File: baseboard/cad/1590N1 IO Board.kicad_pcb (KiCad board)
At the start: 4 copper layers, 100 x 90 mm, 92 parts, among them J1 DC POWER JACK, J10 2P_HEADER, J11 2P_HEADER, J12 6-440054-2, J13 6-440054-2, J17 6-440054-2, J18 6-440054-2, J2 1/4" JACK, STEREO, J3 6-440054-2, J5 1/4" JACK, STEREO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

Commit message: swapped micro and started layout
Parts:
- removed U11, U12: DRV8212P, Package_SON:WSON-8-1EP_2x2mm_P0.5mm_EP0.9x1.6mm
- added C33: 100nF, Capacitor_SMD:C_1206_3216Metric, F.Cu at (123.3, 120.6)
- added C34: 10nF, Capacitor_SMD:C_1206_3216Metric, F.Cu at (125.2, 112.7)
- added C35: 100nF, Capacitor_SMD:C_1206_3216Metric, F.Cu at (127.6, 113.2)
- added C36: 22μF, Capacitor_SMD:C_0805_2012Metric, F.Cu at (129.8, 112.1)
- added D9: PESD12VL2BT,215, Package_TO_SOT_SMD:SOT-23, F.Cu at (121.2, 113.1)
- added J16: Conn_01x04_Pin, Connector_PinHeader_2.54mm:PinHeader_1x04_P2.54mm_Vertical, F.Cu at (117.4, 109.3)
- added SW3: SW_DIP_x01, Button_Switch_SMD:SW_Push_SPST_NO_Alps_SKRK, F.Cu at (133.4, 114.5)
- added U3: DRV8833RTY, Package_DFN_QFN:Texas_S-PWQFN-N16_EP2.1x2.1mm_ThermalVias, F.Cu at (128.0, 107.7)
- added Y1: 830054236, Crystal:Crystal_SMD_3215-2Pin_3.2x1.5mm, F.Cu at (131.2, 123.2)
- U8: footprint Package_DFN_QFN:DFN-10-1EP_3x3mm_P0.5mm_EP1.65x2.38mm -> Package_DFN_QFN:DFN-10-1EP_3x3mm_P0.5mm_EP1.65x2.38mm_ThermalVias
- moved U10 119.6 mm to (128.0, 120.5), turned to 180 degrees
- moved C32 111.8 mm to (132.7, 119.8), turned to 180 degrees
- moved C30 109.9 mm to (134.0, 124.5)
- moved C31 109.3 mm to (134.0, 122.0)
- moved R2 100.3 mm to (109.0, 95.4), turned to -90 degrees
- moved C4 99.9 mm to (107.3, 95.4), turned to 90 degrees
- moved F1 95.2 mm to (124.0, 87.5), turned to 90 degrees
- moved F2 94.1 mm to (126.4, 87.5), turned to 90 degrees
- moved C8 92.2 mm to (111.3, 96.1), turned to -90 degrees
- moved C7 88.9 mm to (113.8, 96.1), turned to -90 degrees
- moved C6 85.6 mm to (116.2, 96.1), turned to -90 degrees
- moved D2 84.7 mm to (124.8, 83.1), turned to -90 degrees
- moved D4 84.4 mm to (130.2, 85.2), turned to 90 degrees
- moved K1 82.0 mm to (123.2, 97.6), turned to 90 degrees
- moved K2 71.7 mm to (132.8, 97.6), turned to 90 degrees
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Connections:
- D1 pad 1: Net-(D1-A1) -> GND
- D2 pad 1: Net-(D2-A1) -> /Input Output/DC_IN+
- D3 pad 1: Net-(D3-A1) -> GND
- D4 pad 3: Net-(D4-+) -> DC_IN
- J1 pad 3: Net-(J1-Pad3) -> /Input Output/BATT_SW_A
- J2 pad R: Net-(J2-PadR) -> /Input Output/BATT_SW_B
- J2 pad RN: Net-(J2-PadR) -> /Input Output/BATT_SW_B
- U10 pad 10: unconnected-(U10-PA7-Pad10) -> +9V_EN
- U10 pad 11: unconnected-(U10-PB1-Pad11) -> -9V_EN
- U10 pad 16: SWDIO -> SWDCK
- U10 pad 17: SWDCK -> SWDIO
- U10 pad 6: /Microcontroller/H-BRIDGE1_IN1 -> /Microcontroller/H-BRIDGE2_IN2
- U10 pad 7: /Microcontroller/H-BRIDGE1_IN2 -> /Microcontroller/H-BRIDGE2_IN1
- U10 pad 8: /Microcontroller/H-BRIDGE2_IN1 -> /Microcontroller/H-BRIDGE1_IN2
- U10 pad 9: /Microcontroller/H-BRIDGE2_IN2 -> /Microcontroller/H-BRIDGE1_IN1
- U9 pad 10: +Vsw -> -9V_EN
- U9 pad 12: +Vsw -> +9V_EN
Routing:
- net SWDIO: track 0.00 -> 25.8 mm
- net /Microcontroller/K1_COIL_A: track 0.00 -> 22.3 mm
- net /Microcontroller/K2_COIL_A: track 0.00 -> 22.3 mm
- net SWDCK: track 0.00 -> 21.3 mm
- net /Microcontroller/H-BRIDGE1_IN1: track 0.00 -> 14.9 mm
- net GND: track 0.00 -> 14.7 mm, vias 0 -> 14
- net /Microcontroller/H-BRIDGE1_IN2: track 0.00 -> 14.1 mm
- net /Microcontroller/H-BRIDGE2_IN2: track 0.00 -> 13.1 mm
- net /Microcontroller/H-BRIDGE2_IN1: track 0.00 -> 12.5 mm
- net /Microcontroller/K2_COIL_B: track 0.00 -> 11.1 mm
- net /Microcontroller/K1_COIL_B: track 0.00 -> 11.1 mm
- net /Input Output/DC_IN+: track 0.00 -> 10.1 mm
- net /Switching/BYPASS_1: track 0.00 -> 9.72 mm
- net /Switching/BYPASS_2: track 0.00 -> 9.72 mm
- net /Input Output/DC_IN_FUSED-: track 0.00 -> 8.54 mm
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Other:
- board size 100 x 90 mm -> 58 x 77 mm
- board text added: "3V3"
- board text added: "CLK"
- board text added: "GND"
- board text added: "IO"
- board text added: "SWD"

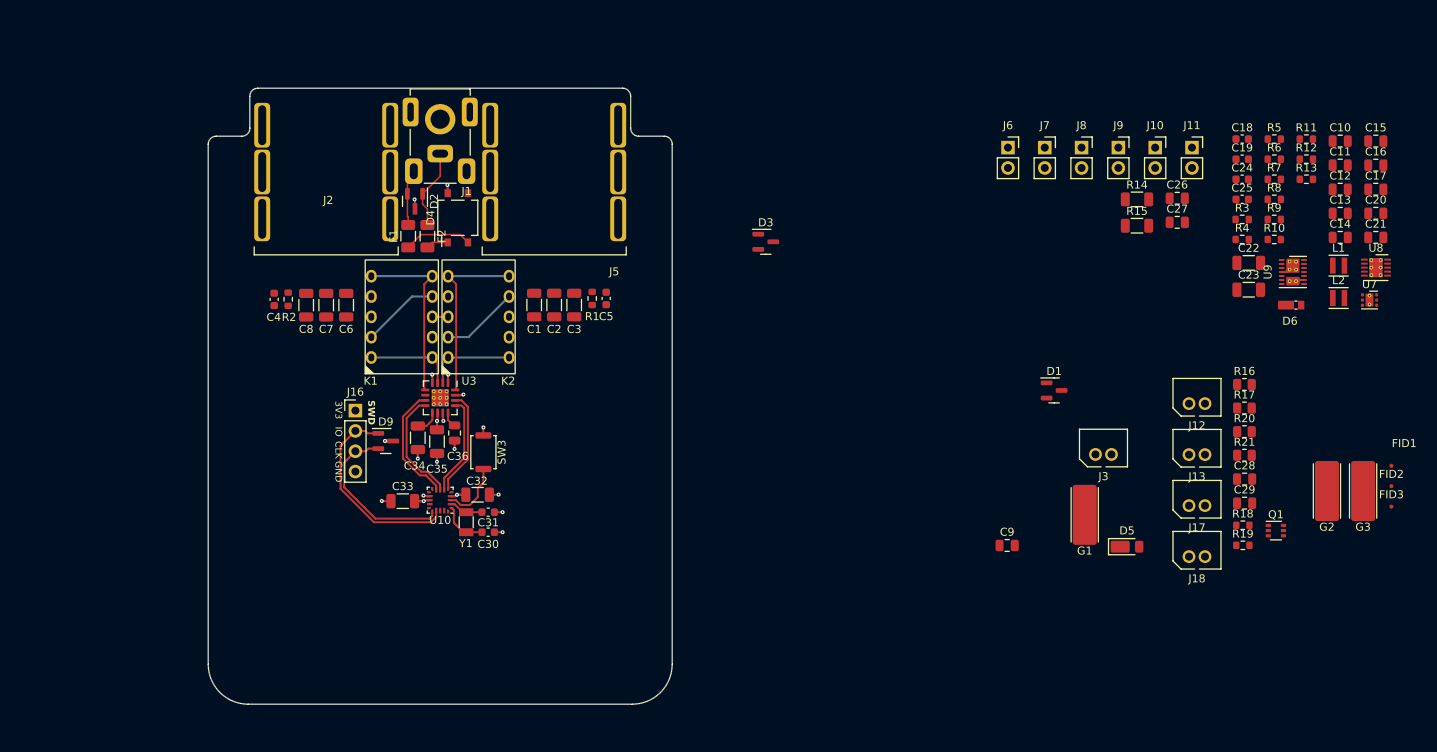
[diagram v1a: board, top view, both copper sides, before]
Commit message: placed components and finished new micro hw
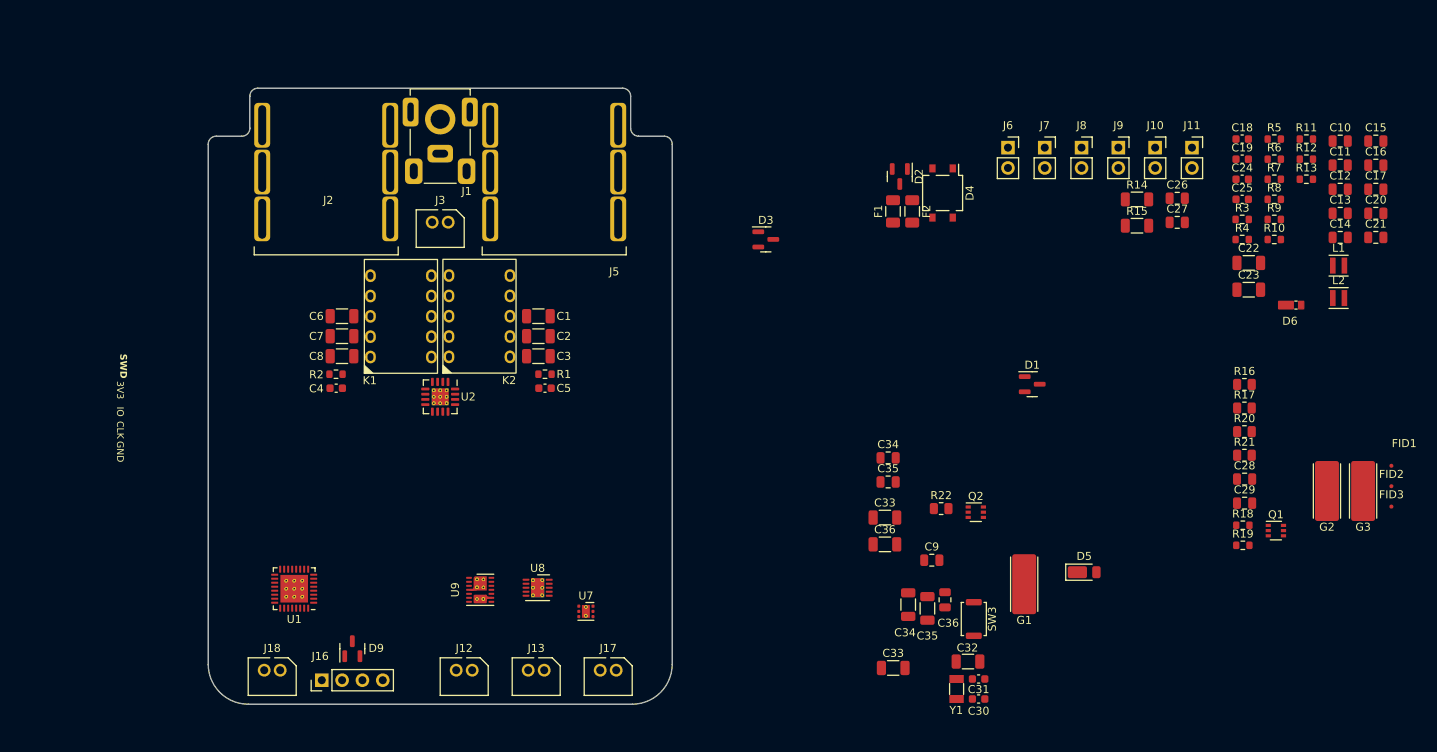
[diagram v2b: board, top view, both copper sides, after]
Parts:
- removed U10: STM32L011F3Ux, Package_DFN_QFN:ST_UFQFPN-20_3x3mm_P0.5mm
- removed U3: DRV8833RTY, Package_DFN_QFN:Texas_S-PWQFN-N16_EP2.1x2.1mm_ThermalVias
- added C33: 10nF, Capacitor_SMD:C_1206_3216Metric, F.Cu at (183.6, 122.7)
- added C34: 22μF, Capacitor_SMD:C_0805_2012Metric, F.Cu at (184.0, 115.2)
- added C35: 2.2μF, Capacitor_SMD:C_0805_2012Metric, F.Cu at (184.0, 118.2)
- added C36: 100nF, Capacitor_SMD:C_1206_3216Metric, F.Cu at (183.6, 126.0)
- added Q2: Q_Dual_NMOS_S1G1D2S2G2D1, Package_TO_SOT_SMD:SOT-363_SC-70-6, F.Cu at (194.9, 122.0)
- added R22: 47Ω, Resistor_SMD:R_0805_2012Metric, F.Cu at (190.6, 121.5)
- added U1: STM32G031K8Ux, Package_DFN_QFN:QFN-32-1EP_5x5mm_P0.5mm_EP3.45x3.45mm_ThermalVias, F.Cu at (109.8, 131.6)
- added U2: DRV8833RTY, Package_DFN_QFN:Texas_S-PWQFN-N16_EP2.1x2.1mm_ThermalVias, F.Cu at (128.0, 107.6)
- moved J18 116.1 mm to (107.0, 140.0), turned to 180 degrees
- moved U8 112.2 mm to (140.2, 131.4)
- moved U9 109.1 mm to (133.0, 131.7)
- moved U7 105.4 mm to (146.2, 134.4)
- moved J12 96.3 mm to (131.0, 140.0), turned to 180 degrees
- moved J3 89.1 mm to (128.0, 84.0), turned to 180 degrees
- moved J13 85.9 mm to (140.0, 140.0), turned to 180 degrees
- moved J17 75.6 mm to (149.0, 140.0), turned to 180 degrees
- moved C30 64.7 mm to (195.3, 145.3)
- moved C31 64.7 mm to (195.3, 142.8)
- moved C35 64.7 mm to (188.9, 134.0)
- moved Y1 64.7 mm to (192.6, 144.1)
- moved C33 64.7 mm to (184.6, 141.5)
- moved C34 64.7 mm to (186.5, 133.6)
- moved C32 64.7 mm to (194.0, 140.7)
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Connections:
- net Net-(U10-PC14) renamed /Microcontroller/MCXO1
- net Net-(U10-PC15) renamed /Microcontroller/MCXO2
- C12 pad 2: +Vsw -> DC_IN
- K1 pad 1: /Microcontroller/K1_COIL_B -> /Microcontroller/K2_COIL_B
- K1 pad 10: /Microcontroller/K1_COIL_A -> /Microcontroller/K2_COIL_A
- K1 pad 5: /Microcontroller/K1_COIL_A -> /Microcontroller/K2_COIL_A
- K1 pad 6: /Microcontroller/K1_COIL_B -> /Microcontroller/K2_COIL_B
- K2 pad 1: /Microcontroller/K2_COIL_B -> /Microcontroller/K1_COIL_B
- K2 pad 10: /Microcontroller/K2_COIL_A -> /Microcontroller/K1_COIL_A
- K2 pad 5: /Microcontroller/K2_COIL_A -> /Microcontroller/K1_COIL_A
- K2 pad 6: /Microcontroller/K2_COIL_B -> /Microcontroller/K1_COIL_B
- U7 pad 4: +Vsw -> DC_IN
- U7 pad 6: +Vsw -> DC_IN
- U8 pad 8: DC_IN -> -12V_EN
- U8 pad 9: DC_IN -> +12V_EN
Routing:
- net SWDIO: track 25.8 -> 0.00 mm
- net /Microcontroller/K1_COIL_A: track 22.3 -> 0.00 mm
- net /Microcontroller/K2_COIL_A: track 22.3 -> 0.00 mm
- net SWDCK: track 21.3 -> 0.00 mm
- net /Microcontroller/H-BRIDGE1_IN1: track 14.9 -> 0.00 mm
- net GND: track 14.7 -> 0.00 mm, vias 14 -> 0
- net /Microcontroller/H-BRIDGE1_IN2: track 14.1 -> 0.00 mm
- net /Microcontroller/H-BRIDGE2_IN2: track 13.1 -> 0.00 mm
- net /Microcontroller/H-BRIDGE2_IN1: track 12.5 -> 0.00 mm
- net /Microcontroller/K2_COIL_B: track 11.1 -> 0.00 mm
- net /Microcontroller/K1_COIL_B: track 11.1 -> 0.00 mm
- net /Input Output/DC_IN+: track 10.1 -> 0.00 mm
- net /Switching/BYPASS_1: track 9.72 -> 0.00 mm
- net /Switching/BYPASS_2: track 9.72 -> 0.00 mm
- net /Input Output/DC_IN_FUSED-: track 8.54 -> 0.00 mm
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
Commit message: updated schematic page setup
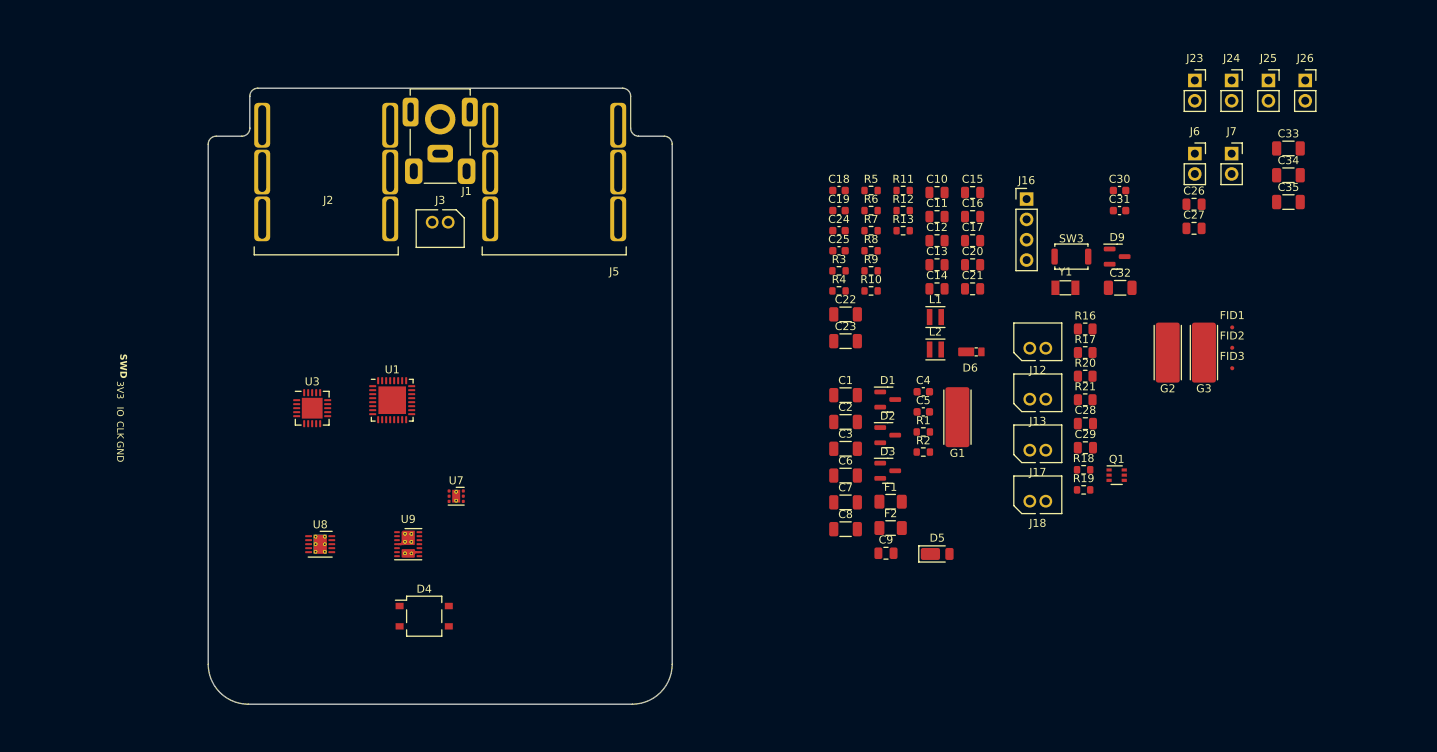
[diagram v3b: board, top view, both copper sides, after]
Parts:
- removed the C33 at (184.6, 141.5)
- removed the C33 at (183.6, 122.7)
- removed the C34 at (186.5, 133.6)
- removed the C34 at (184.0, 115.2)
- removed the C35 at (184.0, 118.2)
- removed the C35 at (188.9, 134.0)
- removed C36: 22μF, Capacitor_SMD:C_0805_2012Metric
- removed C36: 100nF, Capacitor_SMD:C_1206_3216Metric
- removed J10, J11, J8, J9: 2P_HEADER, Connector_PinSocket_2.54mm:PinSocket_1x02_P2.54mm_Vertical
- removed K1, K2: TQ2-L2-3V3, Library:Panasonic_TQ2-L2-5V
- removed Q2: Q_Dual_NMOS_S1G1D2S2G2D1, Package_TO_SOT_SMD:SOT-363_SC-70-6
- removed R14, R15: 0Ω, Resistor_SMD:R_1206_3216Metric
- removed R22: 47Ω, Resistor_SMD:R_0805_2012Metric
- removed U2: DRV8833RTY, Package_DFN_QFN:Texas_S-PWQFN-N16_EP2.1x2.1mm_ThermalVias
- added C33: 100nF, Capacitor_SMD:C_1206_3216Metric, F.Cu at (234.0, 76.5)
- added C34: 100nF, Capacitor_SMD:C_1206_3216Metric, F.Cu at (234.0, 79.9)
- added C35: 100nF, Capacitor_SMD:C_1206_3216Metric, F.Cu at (234.0, 83.2)
- added J23: 2P_HEADER, Connector_PinSocket_2.54mm:PinSocket_1x02_P2.54mm_Vertical, F.Cu at (222.3, 68.0)
- added J24: 2P_HEADER, Connector_PinSocket_2.54mm:PinSocket_1x02_P2.54mm_Vertical, F.Cu at (226.9, 68.0)
- added J25: 2P_HEADER, Connector_PinSocket_2.54mm:PinSocket_1x02_P2.54mm_Vertical, F.Cu at (231.5, 68.0)
- added J26: 2P_HEADER, Connector_PinSocket_2.54mm:PinSocket_1x02_P2.54mm_Vertical, F.Cu at (236.1, 68.0)
- added U3: ADG5434, Package_CSP:LFCSP-20-1EP_4x4mm_P0.5mm_EP2.6x2.6mm, F.Cu at (112.0, 109.0)
- U1: footprint Package_DFN_QFN:QFN-32-1EP_5x5mm_P0.5mm_EP3.45x3.45mm_ThermalVias -> Package_DFN_QFN:QFN-32-1EP_5x5mm_P0.5mm_EP3.45x3.45mm
- moved D9 107.4 mm to (212.6, 90.0), turned to 0 degrees
- moved J16 106.7 mm to (201.3, 82.9), turned to 0 degrees
- moved J18 97.3 mm to (202.7, 122.4), turned to 0 degrees
- moved D4 83.7 mm to (126.0, 135.0), turned to 0 degrees
- moved J12 80.6 mm to (202.7, 103.2), turned to 0 degrees
- moved R2 74.1 mm to (188.4, 114.5)
- moved C4 73.4 mm to (188.4, 107.0), turned to 0 degrees
- moved J13 69.7 mm to (202.7, 109.6), turned to 0 degrees
- moved C8 66.6 mm to (178.7, 124.1)
- moved C7 66.3 mm to (178.7, 120.8)
- moved C6 66.0 mm to (178.7, 117.4)
- moved C30 66.0 mm to (212.9, 81.8)
- moved C31 61.1 mm to (212.9, 84.3)
- moved J17 58.8 mm to (202.7, 116.0), turned to 0 degrees
- moved Y1 52.0 mm to (206.2, 94.0), turned to 0 degrees
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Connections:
- net /Microcontroller/MCXO1 renamed /Microcontroller/XO1
- net /Microcontroller/MCXO2 renamed /Microcontroller/XO2
- U1 pad 10: /Microcontroller/H-BRIDGE_FAULT -> /Microcontroller/SW_EN
- U1 pad 11: /Microcontroller/H-BRIDGE2_IN2 -> /Microcontroller/SW_IN1
- U1 pad 12: /Microcontroller/H-BRIDGE2_IN1 -> /Microcontroller/SW_IN2
- U1 pad 13: /Microcontroller/H-BRIDGE1_IN2 -> /Microcontroller/SW_IN3
- U1 pad 14: /Microcontroller/H-BRIDGE1_IN1 -> /Microcontroller/SW_IN4
- U1 pad 19: +9V_EN -> unconnected-(U1-PA9/NC-Pad19)
- U1 pad 20: -9V_EN -> unconnected-(U1-PC6-Pad20)
- U1 pad 9: /Microcontroller/H-BRIDGE_SLEEP -> unconnected-(U1-PA2-Pad9)
- U9 pad 10: -9V_EN -> +Vsw
- U9 pad 12: +9V_EN -> +Vsw

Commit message: restarted layout
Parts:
- D2: value PESD12VL2BT,215 -> TVS
- moved F1 70.0 mm to (124.8, 83.8), turned to 90 degrees
- moved F2 66.6 mm to (131.2, 83.8), turned to 90 degrees
- moved D2 63.0 mm to (128.0, 83.4), turned to -90 degrees
- moved J3 54.9 mm to (166.0, 123.6)
- moved D4 45.0 mm to (128.0, 90.0), turned to -90 degrees
- moved U8 22.3 mm to (135.2, 128.6)
- moved Q1 19.9 mm to (198.0, 131.0)
- moved U3 17.9 mm to (128.0, 101.0)
- moved U9 16.4 mm to (140.2, 128.4)
- moved U7 16.2 mm to (143.8, 128.4)
- moved U1 8.93 mm to (119.8, 116.7)

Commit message: more early layout work
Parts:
- added C36: 100nF, Capacitor_SMD:C_1206_3216Metric, F.Cu at (196.4, 101.3)
- added U2: 74LVC2G17, Package_TO_SOT_SMD:SOT-363_SC-70-6, F.Cu at (193.2, 92.6)
- D2: value TVS -> PESD12VL2BT,215
- U1: footprint Package_DFN_QFN:QFN-32-1EP_5x5mm_P0.5mm_EP3.45x3.45mm -> Package_DFN_QFN:QFN-32-1EP_5x5mm_P0.5mm_EP3.45x3.45mm_ThermalVias
- moved J25 134.5 mm to (102.3, 105.2), turned to 180 degrees
- moved J23 123.8 mm to (102.2, 98.2), turned to 180 degrees
- moved J16 123.4 mm to (88.4, 132.8), turned to 180 degrees
- moved C31 117.7 mm to (103.9, 128.7), turned to 180 degrees
- moved C30 117.7 mm to (103.9, 126.0), turned to 180 degrees
- moved C34 113.5 mm to (122.5, 101.0), turned to 180 degrees
- moved SW3 111.6 mm to (104.1, 133.6), turned to 90 degrees
- moved C32 110.0 mm to (109.1, 130.2), turned to 90 degrees
- moved C35 108.5 mm to (128.0, 106.2)
- moved Y1 104.9 mm to (106.7, 127.3), turned to 90 degrees
- moved C33 103.5 mm to (133.5, 101.0), turned to 180 degrees
- moved J12 102.2 mm to (107.2, 139.6), turned to 180 degrees
- moved J26 90.4 mm to (153.8, 105.2), turned to 180 degrees
- moved J18 89.4 mm to (115.0, 139.6), turned to 180 degrees
- moved J7 87.2 mm to (153.8, 124.7)
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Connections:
- net /Footswitches/V_FTSW_RAW_A renamed /Peripherals/V_FTSW_RAW_A
- net /Footswitches/V_FTSW_RAW_B renamed /Peripherals/V_FTSW_RAW_B
- net /Footswitches/V_LEDA renamed /Peripherals/V_LEDA
- net /Footswitches/V_LEDB renamed /Peripherals/V_LEDB
- net /Input Output/AUDIO_IN renamed /Input and Output/AUDIO_IN
- net /Input Output/AUDIO_OUT renamed /Input and Output/AUDIO_OUT
- net /Input Output/BATT_SW_A renamed /Input and Output/BATT_SW_A
- net /Input Output/BATT_SW_B renamed /Input and Output/BATT_SW_B
- net /Input Output/DC_IN+ renamed /Input and Output/DC_IN+
- net /Input Output/DC_IN- renamed /Input and Output/DC_IN-
- net /Input Output/DC_IN_FUSED+ renamed /Input and Output/DC_IN_FUSED+
- net /Input Output/DC_IN_FUSED- renamed /Input and Output/DC_IN_FUSED-
- net /Microcontroller/AUDIO_A_TO_B renamed /Microcontroller and Switching/AUDIO_A_TO_B
- net /Microcontroller/BYPASS_A renamed /Microcontroller and Switching/BYPASS_A
- net /Microcontroller/BYPASS_B renamed /Microcontroller and Switching/BYPASS_B
- net /Microcontroller/SW_IN4 renamed Net-(U1-PA7)
- net /Microcontroller/XO1 renamed /Microcontroller and Switching/XO1
- net /Microcontroller/XO2 renamed /Microcontroller and Switching/XO2
- C28 pad 2: V_FTSW_A -> Net-(C28-Pad2)
- C29 pad 2: V_FTSW_B -> Net-(C29-Pad2)
- R16 pad 1: V_FTSW_A -> Net-(C28-Pad2)
- R17 pad 1: V_FTSW_B -> Net-(C29-Pad2)
- R18 pad 1: V_FTSW_A -> Net-(C28-Pad2)
- R19 pad 1: V_FTSW_B -> Net-(C29-Pad2)
- U1 pad 10: /Microcontroller/SW_EN -> Net-(U1-PA3)
- U1 pad 11: /Microcontroller/SW_IN1 -> Net-(U1-PA4)
- U1 pad 12: /Microcontroller/SW_IN2 -> Net-(U1-PA5)
- U1 pad 13: /Microcontroller/SW_IN3 -> Net-(U1-PA6)
- U3 pad 18: /Microcontroller/SW_EN -> Net-(U1-PA6)
- U3 pad 19: /Microcontroller/SW_IN1 -> Net-(U1-PA5)
- U3 pad 8: /Microcontroller/SW_IN2 -> Net-(U1-PA3)
- U3 pad 9: /Microcontroller/SW_IN3 -> Net-(U1-PA4)
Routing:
- net /Input and Output/AUDIO_OUT: track 0.00 -> 57.2 mm
- net Net-(U1-PA4): track 0.00 -> 55.7 mm, vias 0 -> 2
- net Net-(U1-PA3): track 0.00 -> 55.6 mm, vias 0 -> 2
- net /Input and Output/AUDIO_IN: track 0.00 -> 54.2 mm
- net GND: track 0.00 -> 51.6 mm, vias 0 -> 19
- net Net-(U1-PA5): track 0.00 -> 49.1 mm, vias 0 -> 2
- net Net-(U1-PA6): track 0.00 -> 48.9 mm, vias 0 -> 2
- net Net-(U1-PA7): track 0.00 -> 48.8 mm, vias 0 -> 2
- net DC_IN: track 0.00 -> 38.2 mm, vias 0 -> 2
- net /Input and Output/BATT_SW_B: track 0.00 -> 30.5 mm
- net AUDIO_IN_FILT: track 0.00 -> 16.4 mm
- net AUDIO_OUT_FILT: track 0.00 -> 16.3 mm
- net /Input and Output/BATT_SW_A: track 0.00 -> 16.1 mm
- net -9V: track 0.00 -> 12.1 mm, vias 0 -> 2
- net +9V: track 0.00 -> 9.79 mm, vias 0 -> 2
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- added copper zone on B.Cu, net DC_IN
- added copper zone on F.Cu, net DC_IN
- added copper zone on B.Cu, net GND
- added copper zone on F.Cu, net GND
- added copper zone on In2.Cu, net GND
- removed copper zone on In2.Cu, net +3V3
